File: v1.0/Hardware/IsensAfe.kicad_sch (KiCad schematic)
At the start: 37 parts, among them Q15 MMBT3904, Q16 MMBT3904, U13 L78L05_SOT89, U3 MCP6024, U4 ACPL-7900, U5 TL431LP

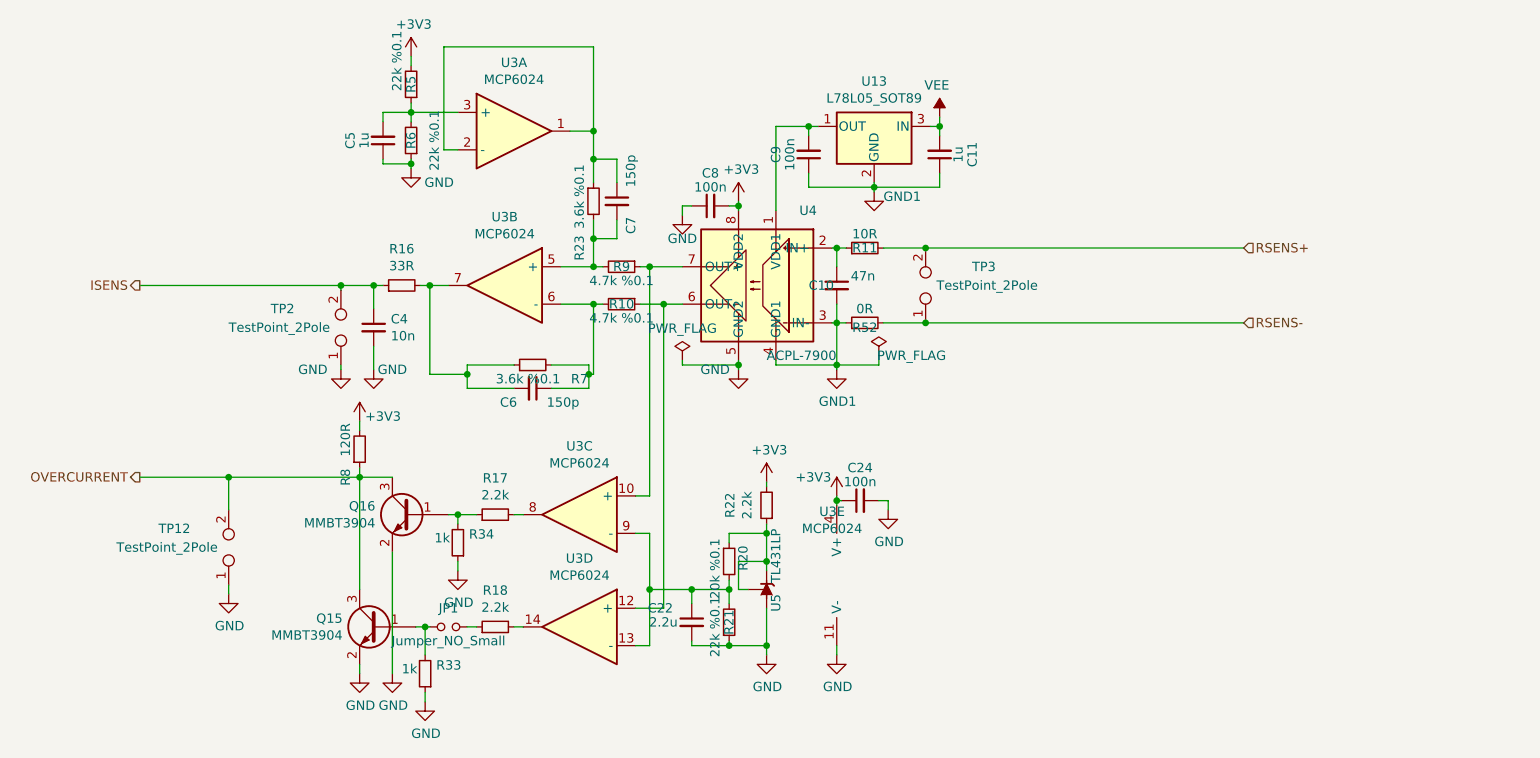
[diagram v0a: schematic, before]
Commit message: v1.1&v1.2 PCB addition.
#####v1.1#####
+Change of MCU; STM32F334C8T6 instead of STM32F103C8T6.
+Filtering 3rd order components of the square wave.
+Use  4 capacitors.
+Adapted to generic transformer(primary 6.4mH, secondary 14.4mH)
+Faster IGBT.

########v1.2#######
+Measures only PZT current and voltage.
+Differential inputs.
+Analog circuitry is capable of measuring four quadrant voltage, current and complex impedance.
+Half bridge configuration.
+Gate resistance of the IGBT's lowered.
+Only USART based touch panel can be connected; not conventional LCD.
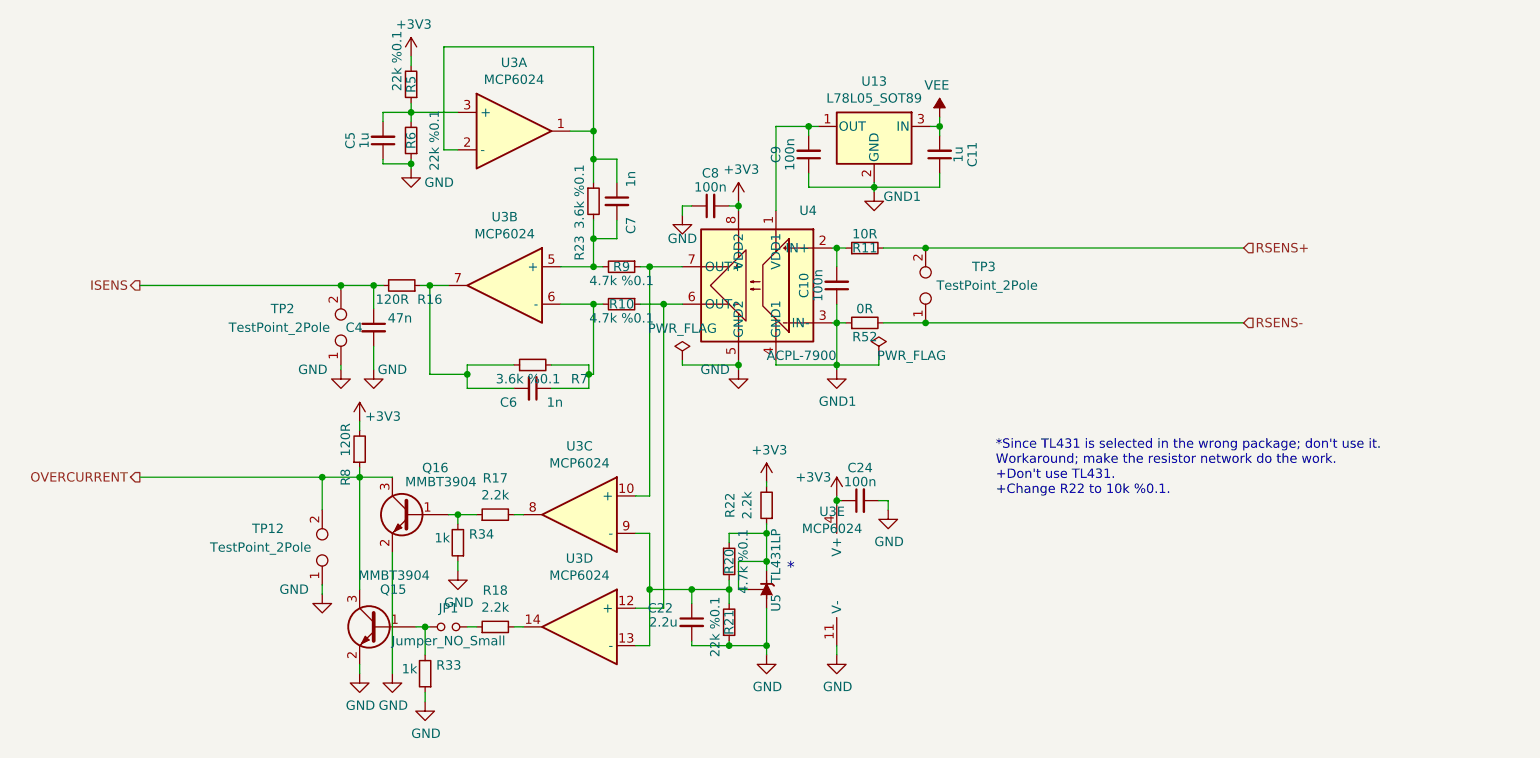
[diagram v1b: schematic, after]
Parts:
- C10: value 47n -> 100n; Link https://ozdisan.com/passive-components/capacitors/smt-smd-and-mlcc-capacitors/CL21B473KBANNNC -> https://ozdisan.com/passive-components/capacitors/smt-smd-and-mlcc-capacitors/CL21B104KBFWPNE; Price 0.08757TL -> 0.10509TL
- C4: value 10n -> 47n; footprint Resistor_SMD:R_0805_2012Metric_Pad1.15x1.40mm_HandSolder -> Capacitor_SMD:C_0805_2012Metric_Pad1.15x1.40mm_HandSolder; Link https://ozdisan.com/passive-components/capacitors/smt-smd-and-mlcc-capacitors/CL21B103KCANNNC -> https://ozdisan.com/passive-components/capacitors/smt-smd-and-mlcc-capacitors/CL21B473KBANNNC; Price 0.05749TL -> 0.08757TL
- C6, C7: value 150p -> 1n; Link https://ozdisan.com/passive-components/capacitors/smt-smd-a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 -> (none); Price 0.09416TL -> (none)
- R16: value 33R -> 120R; Link https://ozdisan.com/passive-components/resistors/smt-smd-and-chip-resistors/0805S8J0330T5E -> https://ozdisan.com/passive-components/resistors/smt-smd-and-chip-resistors/0805S8J0121T5E; Price 0.01504TL -> 0.01492TL
- R20: value 20k %0.1 -> 4.7k %0.1; Link https://ozdisan.com/passive-components/resistors/smt-smd-and-chip-resistors/TC0525B2002T5F -> https://ozdisan.com/passive-components/resistors/smt-smd-and-chip-resistors/TC0525B4701T5F; Price 0.61119TL -> 0.61718TL
- R52: Link https://ozdisan.com/passive-components/resistors/smt-smd-an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 -> (none); Price 0.01492TL -> (none)
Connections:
- net GND1: now also C10.1; no longer C10.2
- net ISENS: now also R16.2; no longer R16.1
- net at R11.1, U4.2 (IN+): now also C10.2; no longer C10.1
- net at C6.2, R7.1, U3.7: now also R16.1; no longer R16.2
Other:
- note added: "*"
- note added: "*Since TL431 is selected in the wrong package; don't use it. Workaround; make the resistor network do the work. +Don't use TL431. +Change R22 to 10k %0.1."
- moved on the sheet: TP12
